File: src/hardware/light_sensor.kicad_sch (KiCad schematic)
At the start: 2 parts, among them U36 LTR-329ALS-01

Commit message: Selected S1..10 & TR1
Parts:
- C102: footprint (none) -> Capacitor_SMD:C_0603_1608Metric
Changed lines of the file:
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@@
 			)
 		)
-		(property "Footprint" ""
+		(property "Footprint" "Capacitor_SMD:C_0603_1608Metric"
 			(at 166.0652 104.14 0)
 			(effects

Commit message: Changed footprints from 0603 to 0402
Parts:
- C102: footprint Capacitor_SMD:C_0603_1608Metric -> Capacitor_SMD:C_0504_1310Metric
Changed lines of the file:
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@@
 			)
 		)
-		(property "Footprint" "Capacitor_SMD:C_0603_1608Metric"
+		(property "Footprint" "Capacitor_SMD:C_0504_1310Metric"
 			(at 166.0652 104.14 0)
 			(effects

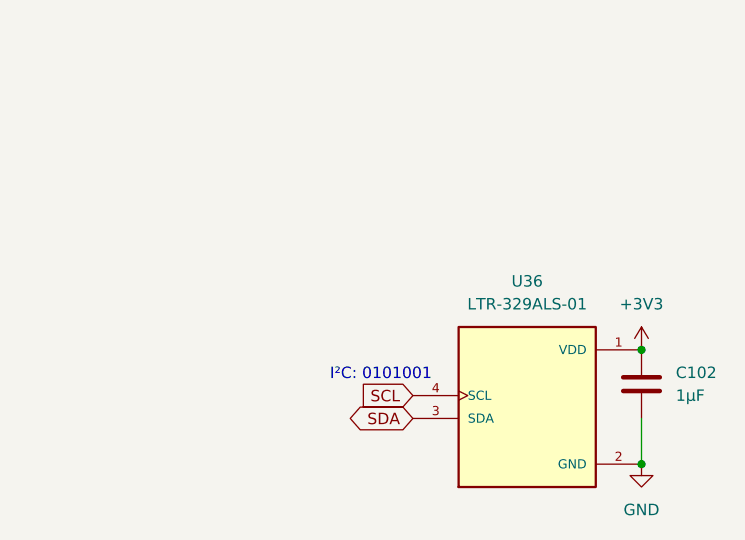
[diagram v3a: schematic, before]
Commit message: Replaced global labels with pin headers
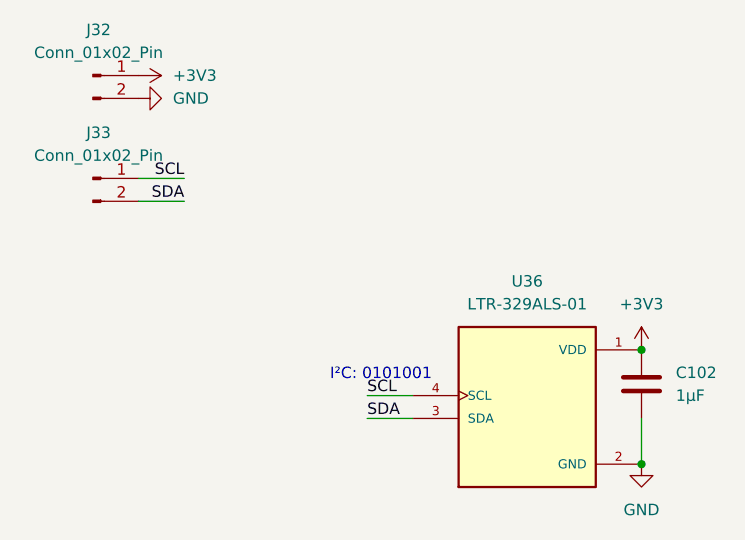
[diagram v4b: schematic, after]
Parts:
- added J32, J33: Conn_01x02_Pin, symbol Connector:Conn_01x02_Pin
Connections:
- net +3V3: now also J32.1 (Pin_1)
- net GND: now also J32.2 (Pin_2)
- net SCL: now also J33.1 (Pin_1)
- net SDA: now also J33.2 (Pin_2)

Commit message: Reannotated schematic
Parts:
- renumbered C102 to C60, J32 to J67, J33 to J68, U36 to U24
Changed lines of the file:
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@@
 		(dnp no)
 		(fields_autoplaced yes)
-		(property "Reference" "C102"
+		(property "Reference" "C60"
 			(at 168.91 99.0599 0)
 			(effects
@@
 			(project "raywatch"
 				(path "/7b654ee8-2a53-4d39-8b7d-32c7bb3cb0ed/d5a2fc90-5630-482b-949a-d1a5e12221d9"
-					(reference "C102")
+					(reference "C60")
 					(unit 1)
 				)
@@
 		(dnp no)
 		(fields_autoplaced yes)
-		(property "Reference" "U36"
+		(property "Reference" "U24"
 			(at 152.4 88.9 0)
 			(effects
@@
 			(project "raywatch"
 				(path "/7b654ee8-2a53-4d39-8b7d-32c7bb3cb0ed/d5a2fc90-5630-482b-949a-d1a5e12221d9"
-					(reference "U36")
+					(reference "U24")
 					(unit 1)
 				)
@@
 		(dnp no)
 		(fields_autoplaced yes)
-		(property "Reference" "#PWR0415"
+		(property "Reference" "#PWR0362"
 			(at 165.1 115.57 0)
 			(effects
@@
 			(project "raywatch"
 				(path "/7b654ee8-2a53-4d39-8b7d-32c7bb3cb0ed/d5a2fc90-5630-482b-949a-d1a5e12221d9"
-					(reference "#PWR0415")
+					(reference "#PWR0362")
 					(unit 1)
 				)
@@
 		(dnp no)
 		(fields_autoplaced yes)
-		(property "Reference" "#PWR0467"
+		(property "Reference" "#PWR0359"
 			(at 105.41 66.04 0)
 			(effects
@@
 			(project "raywatch"
 				(path "/7b654ee8-2a53-4d39-8b7d-32c7bb3cb0ed/d5a2fc90-5630-482b-949a-d1a5e12221d9"
-					(reference "#PWR0467")
+					(reference "#PWR0359")
 					(unit 1)
 				)
@@
 		(dnp no)
 		(fields_autoplaced yes)
-		(property "Reference" "#PWR0414"
+		(property "Reference" "#PWR0361"
 			(at 165.1 100.33 0)
 			(effects
@@
 			(project "raywatch"
 				(path "/7b654ee8-2a53-4d39-8b7d-32c7bb3cb0ed/d5a2fc90-5630-482b-949a-d1a5e12221d9"
-					(reference "#PWR0414")
+					(reference "#PWR0361")
 					(unit 1)
 				)
@@
 		(dnp no)
 		(fields_autoplaced yes)
-		(property "Reference" "J33"
+		(property "Reference" "J68"
 			(at 104.775 72.39 0)
 			(effects
@@
 			(project "raywatch"
 				(path "/7b654ee8-2a53-4d39-8b7d-32c7bb3cb0ed/d5a2fc90-5630-482b-949a-d1a5e12221d9"
-					(reference "J33")
+					(reference "J68")
 					(unit 1)
 				)
@@
 		(dnp no)
 		(fields_autoplaced yes)
-		(property "Reference" "#PWR0468"
+		(property "Reference" "#PWR0360"
 			(at 115.57 68.58 0)
 			(effects
@@
 			(project "raywatch"
 				(path "/7b654ee8-2a53-4d39-8b7d-32c7bb3cb0ed/d5a2fc90-5630-482b-949a-d1a5e12221d9"
-					(reference "#PWR0468")
+					(reference "#PWR0360")
 					(unit 1)
 				)
@@
 		(dnp no)
 		(fields_autoplaced yes)
-		(property "Reference" "J32"
+		(property "Reference" "J67"
 			(at 104.775 60.96 0)
 			(effects
@@
 			(project "raywatch"
 				(path "/7b654ee8-2a53-4d39-8b7d-32c7bb3cb0ed/d5a2fc90-5630-482b-949a-d1a5e12221d9"
-					(reference "J32")
-					(unit 1)
-				)
+					(reference "J67")
+					(unit 1)
+				)

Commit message: Assigned pin header footprints
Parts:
- J67, J68: footprint (none) -> Connector_PinHeader_2.54mm:PinHeader_1x02_P2.54mm_Horizontal
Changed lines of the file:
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@@
 			)
 		)
-		(property "Footprint" ""
+		(property "Footprint" "Connector_PinHeader_2.54mm:PinHeader_1x02_P2.54mm_Horizontal"
 			(at 104.14 77.47 0)
 			(effects
@@
 			)
 		)
-		(property "Footprint" ""
+		(property "Footprint" "Connector_PinHeader_2.54mm:PinHeader_1x02_P2.54mm_Horizontal"
 			(at 104.14 66.04 0)
 			(effects

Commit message: Changed pin headers to vertical
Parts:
- J67, J68: footprint Connector_PinHeader_2.54mm:PinHeader_1x02_P2.54mm_Horizontal -> Connector_PinHeader_2.54mm:PinHeader_1x02_P2.54mm_Vertical
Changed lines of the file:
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@@
 			)
 		)
-		(property "Footprint" "Connector_PinHeader_2.54mm:PinHeader_1x02_P2.54mm_Horizontal"
+		(property "Footprint" "Connector_PinHeader_2.54mm:PinHeader_1x02_P2.54mm_Vertical"
 			(at 104.14 77.47 0)
 			(effects
@@
 			)
 		)
-		(property "Footprint" "Connector_PinHeader_2.54mm:PinHeader_1x02_P2.54mm_Horizontal"
+		(property "Footprint" "Connector_PinHeader_2.54mm:PinHeader_1x02_P2.54mm_Vertical"
 			(at 104.14 66.04 0)
 			(effects
